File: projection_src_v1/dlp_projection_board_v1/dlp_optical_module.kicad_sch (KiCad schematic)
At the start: 1 part, among them U4 DLP3010AFQK

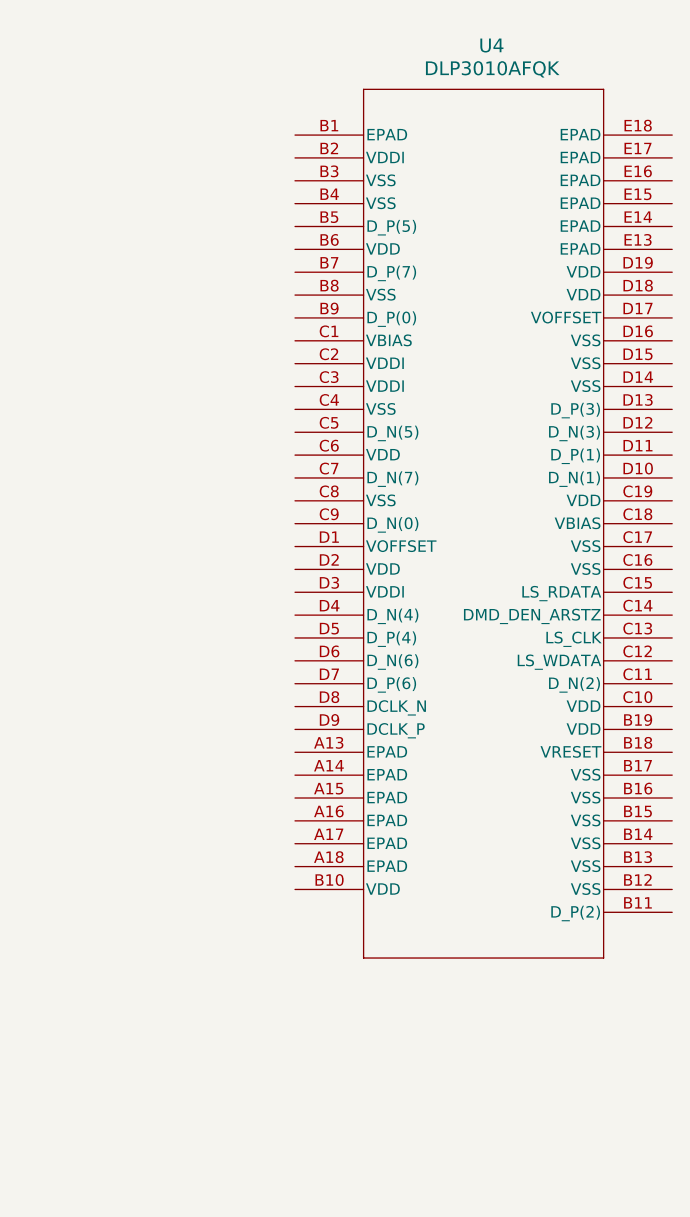
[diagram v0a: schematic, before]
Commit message: Added schematic template
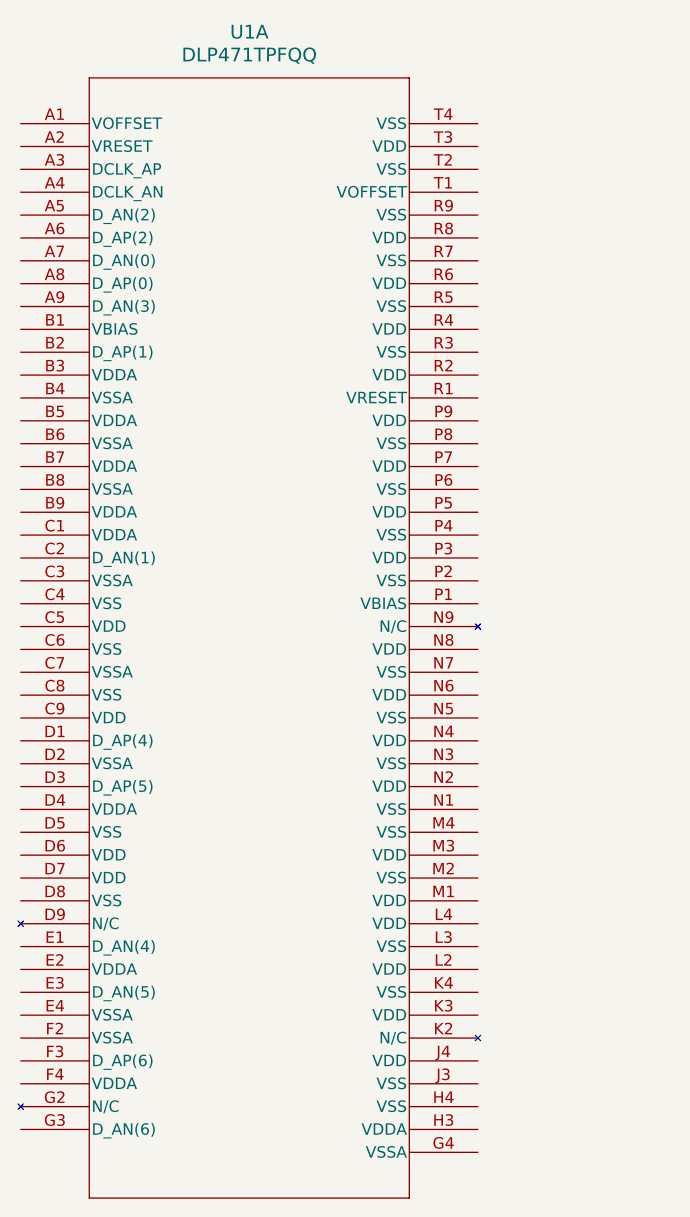
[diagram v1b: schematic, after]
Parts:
- removed U4: DLP3010AFQK, FQK57_TEX, symbol DLP3010:DLP3010AFQK
- added U1: DLP471TPFQQ, CLGA250_FQN_TEX, symbol 471TP:DLP471TPFQQ
